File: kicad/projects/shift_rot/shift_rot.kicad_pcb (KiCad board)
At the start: 2 copper layers, 203.2 x 97.8 mm, 68 parts, among them J4 Conn_01x03_Pin, J5 Conn_01x16_Socket, J6 Conn_01x02_Socket, J7 Control_signal_backplane, J8 Bus_connection, J9 Aux_connection, U10 74HC08, U11 74HC574, U12 74HC574, U13 74HC138, U14 74HC157, U16 74HC245, U17 74HC245, U18 74HC02, U19 74HC00, U20 74HC377, U21 74HC377, U3 74HC245, U4 74HC245, U5 74HC245, U6 74HC245, U7 74HC245, U8 74HC245, U9 74HC157

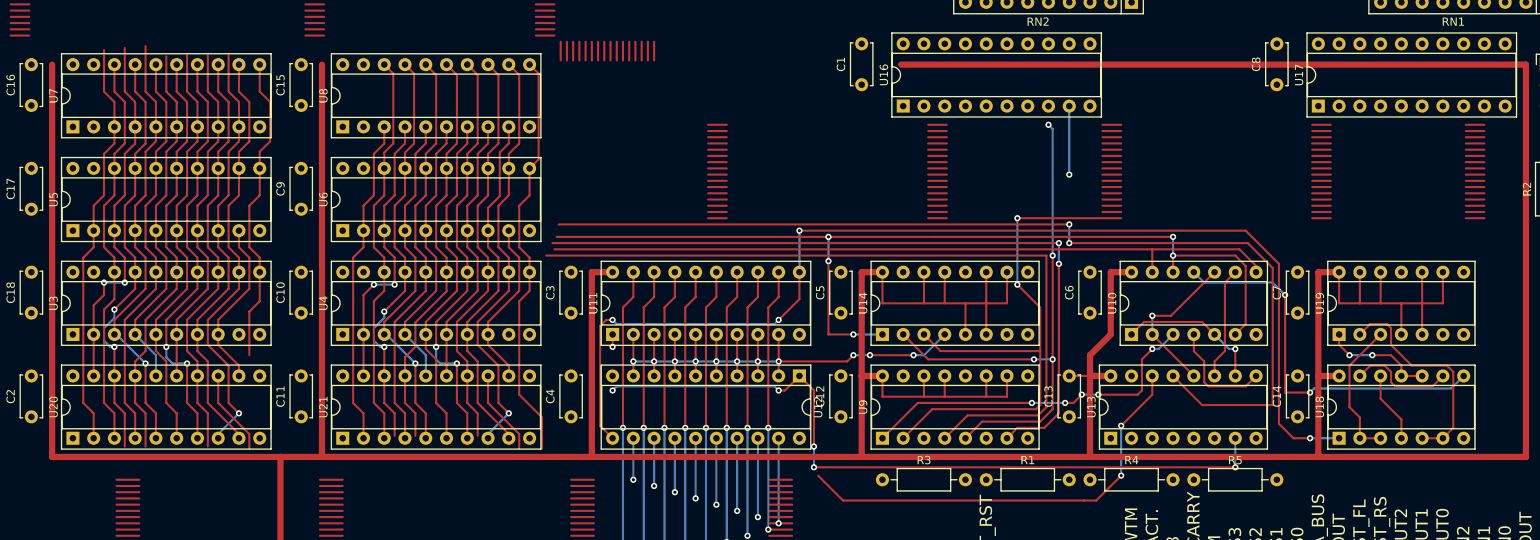
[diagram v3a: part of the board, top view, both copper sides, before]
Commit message: More work on shift rot PCB
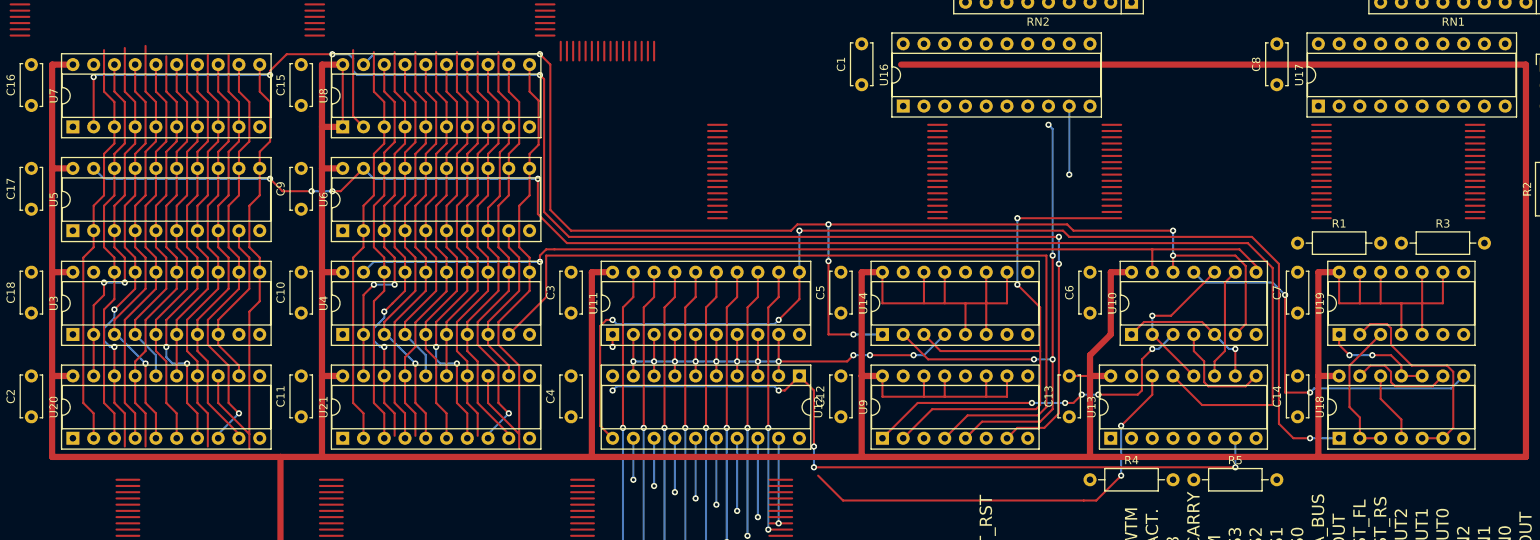
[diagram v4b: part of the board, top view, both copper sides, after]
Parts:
- moved R3 69.8 mm to (223.5, 100.6)
- moved R1 47.9 mm to (210.8, 100.6)
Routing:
- net /RIGHT_MSB: track 90.4 -> 174.5 mm, vias 2 -> 6
- net /~{STRAIGHT_OUT}: track 121.4 -> 184.6 mm, vias 2 -> 4
- net /~{EITHER_RIGHT_OUT}: track 116.6 -> 163.0 mm, vias 5 -> 6
- net VCC: track 642.4 -> 672.9 mm
- net /~{EITHER_LEFT_OUT}: track 90.2 -> 115.2 mm, vias 0 -> 1
- net /LEFT_LSB: track 93.8 -> 105.3 mm
- net /CNTNT_8: track 49.9 -> 59.8 mm
- net /CNTNT_2: track 54.2 -> 63.9 mm
- net /CNTNT_4: track 55.8 -> 65.4 mm
- net /CNTNT_5: track 64.1 -> 73.8 mm
- net /CNTNT_3: track 63.1 -> 72.8 mm
- net /CNTNT_1: track 63.9 -> 73.6 mm
- net /CNTNT_7: track 60.8 -> 70.4 mm
- net /CNTNT_6: track 55.7 -> 65.4 mm
- net /BUS_8: track 92.0 -> 101.6 mm
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
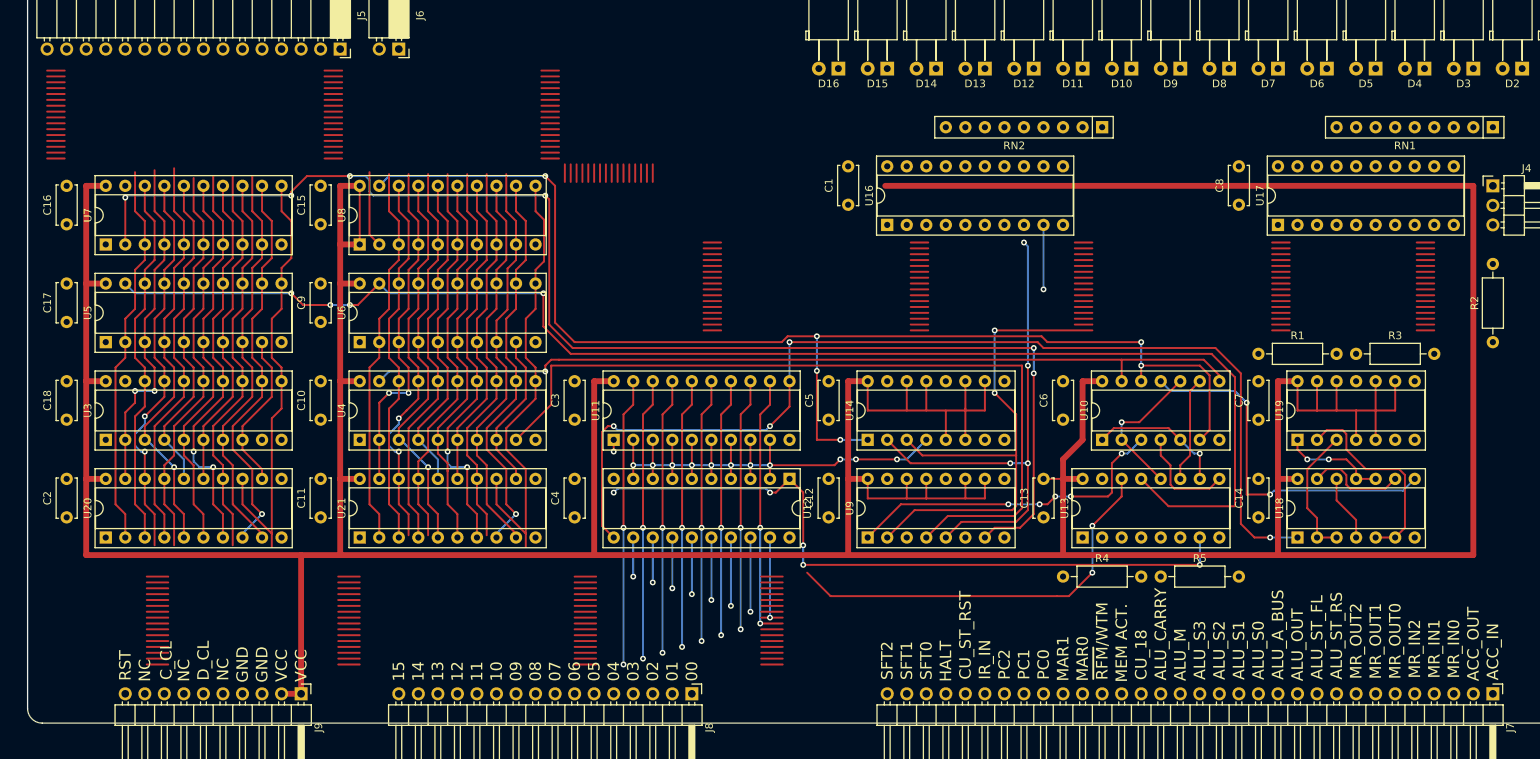
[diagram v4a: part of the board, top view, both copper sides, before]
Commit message: More work on shift rot PCB
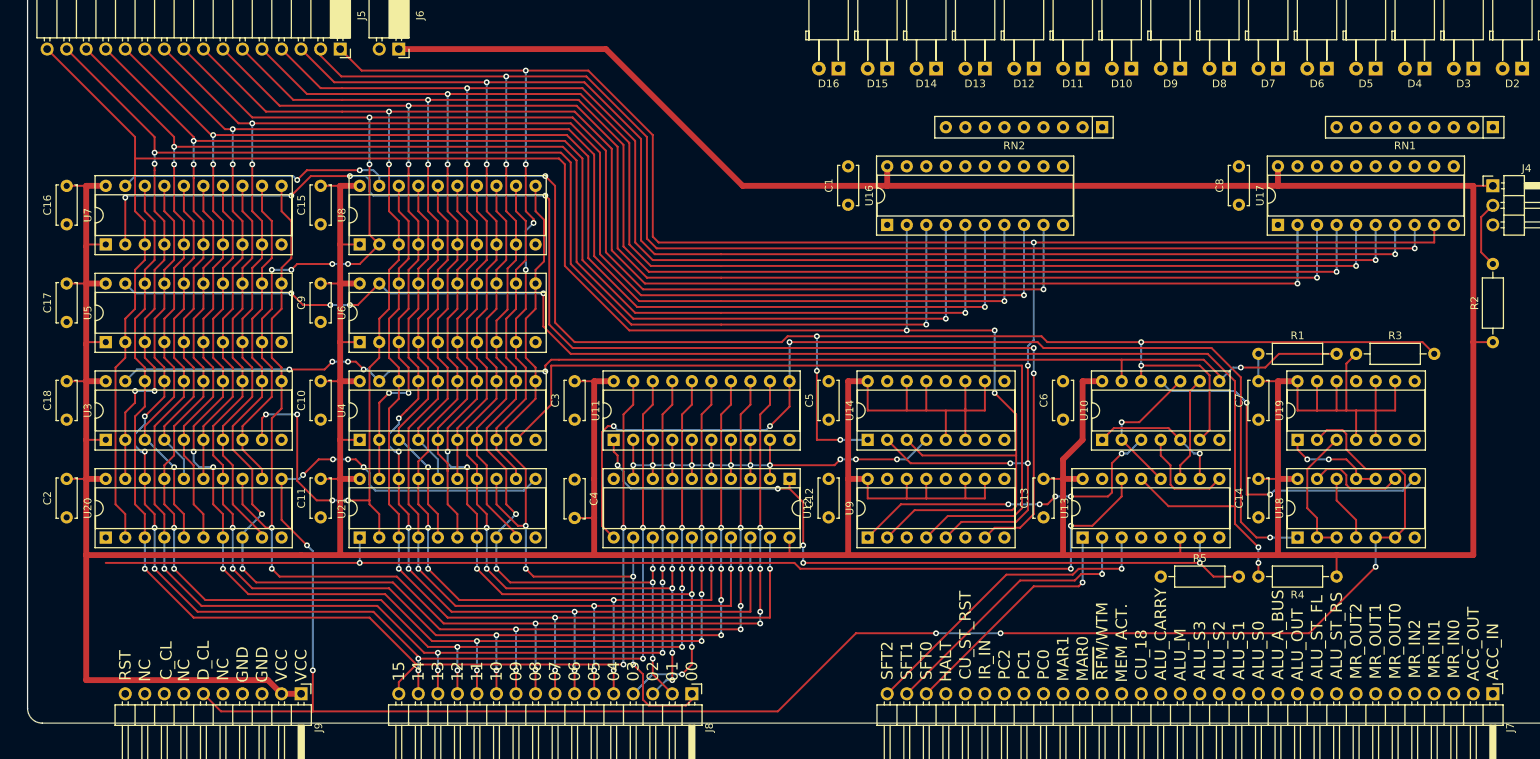
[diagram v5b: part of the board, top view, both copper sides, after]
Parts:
- moved R4 35.6 mm to (221.0, 129.5), turned to 180 degrees
- moved C4 4.92 mm to (121.9, 116.9), turned to -90 degrees
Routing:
- net /DATA_CLK: track 26.8 -> 260.9 mm, vias 0 -> 9
- net /CNTNT_7: track 70.4 -> 255.1 mm, vias 0 -> 7
- net /CNTNT_0: track 108.2 -> 287.1 mm, vias 4 -> 8
- net VCC: track 672.9 -> 832.6 mm
- net /CNTNT_6: track 65.4 -> 222.8 mm, vias 2 -> 5
- net /CNTNT_5: track 73.8 -> 230.9 mm, vias 1 -> 4
- net /CNTNT_4: track 65.4 -> 222.3 mm, vias 0 -> 3
- net /CNTNT_3: track 72.8 -> 229.3 mm, vias 0 -> 3
- net /CNTNT_1: track 73.6 -> 230.0 mm, vias 0 -> 3
- net /CNTNT_2: track 63.9 -> 220.1 mm, vias 0 -> 3
- net /CNTNT_8: track 59.8 -> 204.1 mm, vias 1 -> 7
- net /CNTNT_15: track 138.6 -> 270.9 mm, vias 2 -> 3
- net /CNTNT_14: track 65.9 -> 196.1 mm, vias 2 -> 5
- net /CNTNT_12: track 64.4 -> 194.1 mm, vias 0 -> 3
- net /CNTNT_13: track 74.8 -> 203.9 mm, vias 1 -> 4
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
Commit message: Almost done on shift rot PCB.
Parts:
- moved C98 232.9 mm to (243.9, 124.5)
- moved C97 119.3 mm to (55.9, 137.1), turned to 90 degrees
- moved C99 115.9 mm to (149.9, 76.2)
- moved RN1 1.27 mm to (240.0, 71.1)
- moved RN2 1.27 mm to (189.2, 71.1)
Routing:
- net Net-(J4-Pin_2): track 8.88 -> 96.9 mm
- net VCC: track 832.6 -> 873.5 mm, vias 0 -> 1
- net Net-(D9-A): track 0.00 -> 24.1 mm
- net Net-(D1-A): track 0.00 -> 23.0 mm
- net Net-(D16-A): track 0.00 -> 22.1 mm
- net Net-(D8-A): track 0.00 -> 21.9 mm
- net Net-(D7-A): track 0.00 -> 20.6 mm
- net Net-(D15-A): track 0.00 -> 20.5 mm
- net Net-(D10-A): track 0.00 -> 20.3 mm
- net Net-(D2-A): track 0.00 -> 19.8 mm
- net Net-(D9-K): track 0.00 -> 19.7 mm
- net Net-(D1-K): track 0.00 -> 18.3 mm
- net Net-(D8-K): track 0.00 -> 17.3 mm
- net Net-(D6-A): track 0.00 -> 16.8 mm
- net Net-(D16-K): track 0.00 -> 16.7 mm
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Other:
- board text added: "0"
- board text added: "1"
- board text added: "10"
- board text added: "11"
- board text added: "12"
- board text added: "13"
- board text added: "14"
- board text added: "15"
- board text added: "2"
- board text added: "3"
- board text added: "4"
- board text added: "5"
- board text added: "6"
- board text added: "7"
- board text added: "8"
- board text added: "9"
- board text added: "GND"
- board text added: "VCC"
